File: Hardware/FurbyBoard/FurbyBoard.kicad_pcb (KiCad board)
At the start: 4 copper layers, 68.8 x 74.6 mm, 154 parts, among them J1 USB-C 16P, J11 J_EXP: header de expansión 2 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, J2 BAT+, J3 BAT-, J5 Micro I2S (SD, GND, SCK, WS, 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, J6 FPC 24P 0.5, J7 Frente: IR (emisor ×2, recept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, J8 Inclinación ×3, lengua ×2, al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, J9 Encoder ×3, leva ×2, barriga 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, Q1 SI7615ADN, Q3 AO3400A, SW1 RESET, SW2 BOOT, U1 USBLC6-2SC6, U10 TCA9535PWR, U11 SN74LVC1G17DBVR, U2 BQ24073RGTR, U3 TPS63802DLAR, U4 ESP32-S3-WROOM-1-N16R8, U5 TPS61089RNRR, U6 DRV8231ADSGR, U7 MAX98357AETE+T, U8 ME6211C28M5G-N, U9 ME6211C12M5G-N

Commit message: Feature: rutado de los sensores de J8 (TILT_A, TILT_B, TONGUE, sus series y el 3V3 de sus pull-ups)
- Bloque RC junto a U10: columna izquierda 0,3 mm al oeste para que quepa una columna de vías
  de 0,6 entre columnas (x -97,15); filas reordenadas (TILT_A, TILT_B, TONGUE) y cinco piezas a 180°.
- TILT_A por el hueco de filas y -78,25 y el pasillo junto a U10 a U10.4; TILT_B recto por y -80,015
  a U10.5; TONGUE por y -81,65 a U10.6. Series TILT_A_PAD, TILT_B_PAD y TONGUE_PAD por vías a B.Cu
  con carriles anidados hasta J8.1, J8.2 y J8.4.
- 3V3 de R45 a R38.2 (0,4 mm por el hueco de 0,75: dos avisos de 0,175 aceptados); R47 y R43 por
  vías a In2 hasta el tronco de 3V3 de B.Cu. TP14 (GND) a (-98,3; -86,4) para liberar B.Cu.

Puerta D: revisar-rutado 0 errores (86 avisos: cuellos, entradas asimétricas y rodeos heredados,
más 3 roces de 0,175-0,2 del 3V3 de R45), DRC paridad 0 y solo las 5 vías colgantes de redes
pendientes (CAM_EN, CAM_PWDN, I2C a J6); 68 sin unir. PNG revisado: zona U10/J8 (mapa con rejilla).

Co-Authored-By: Claude Opus 5.5 (1M context) <noreply@anthropic.com>
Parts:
- moved TP14 7.42 mm to (121.7, 46.4)
- moved C35 4.67 mm to (124.6, 40.8), turned to 180 degrees
- moved C36 3.89 mm to (121.1, 39.1), turned to 180 degrees
- moved R46 3.89 mm to (121.1, 37.4)
- moved R43 3.62 mm to (124.6, 42.5), turned to 180 degrees
- moved R44 3.62 mm to (124.6, 44.2), turned to 180 degrees
- moved C37 3.41 mm to (121.1, 42.5)
- moved R48 3.41 mm to (121.1, 40.8)
- moved R47 3.40 mm to (124.6, 39.1), turned to 180 degrees
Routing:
- net 3V3: track 210.8 -> 237.0 mm, vias 15 -> 18
- net TILT_B_PAD: track 0.00 -> 13.1 mm, vias 0 -> 1
- net TILT_A_PAD: track 0.00 -> 12.3 mm, vias 0 -> 1
- net TONGUE_PAD: track 0.00 -> 11.5 mm, vias 0 -> 1
- net TILT_A: track 0.00 -> 10.6 mm
- net TILT_B: track 0.00 -> 10.5 mm
- net TONGUE: track 0.00 -> 6.31 mm
- net GND: track 86.1 -> 85.2 mm, vias 102 -> 101
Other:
- board text removed: "SD"
- board text removed: "WS"

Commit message: Feature: rutado de los LED del frente, ENC_LED_A, BAT_G y 3V3 locales (R57/R58/R19, R17, TP6)
- LED PWR/RUN/PROG: ánodos rectos a su resistencia; LED_PWR_K por el norte de los LED (y -61,7,
  fuera del área de la antena) y x -52,9 hasta JP5.1.
- 3V3 de R57/R58/R19 por una fila de 0,4 (y -66,0) con vía a In2 (x -55,0) hasta la fila de 3V3
  de In2; la vía de GND de SW2.2 pasa al este (1,5 mm) para dejar sitio. R17.2 al 3V3 de C9/U4.2;
  TP6 unido al tronco de B.Cu (que acababa en y -107,3).
- ENC_LED_A entre las columnas de J9 hasta J9.3. BAT_G de la puerta de Q1 a R12 (0,5 mm dentro
  del patio de Q1 por la regla «cuello Q1»).

Puerta D: revisar-rutado 0 errores (102 avisos; nuevos: 2 roces de 0,15 de LED_PWR_K con D3.1
y JP5.2), DRC paridad 0 y 0 infracciones salvo las 5 vías colgantes de redes pendientes;
57 sin unir. PNG revisados: zona LED/JP5 y zona Q1/R12.

Co-Authored-By: Claude Opus 5.5 (1M context) <noreply@anthropic.com>
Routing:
- net 3V3: track 237.0 -> 269.5 mm, vias 18 -> 19
- net LED_PWR_K: track 0.00 -> 18.4 mm
- net ENC_LED_A: track 0.00 -> 8.81 mm
- net BAT_G: track 0.00 -> 2.80 mm
- net LED_RUN_A: track 0.00 -> 1.95 mm
- net LED_PWR_A: track 0.00 -> 1.95 mm
- net LED_PROG_A: track 0.00 -> 1.92 mm

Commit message: Feature: FurbyBoard a 6 capas (JLC06161H-7628) conservando el rutado: In3 señal, In4 GND, apilado en el PCB y en NOTAS
Decisión de Guillermo (2026-10-24 23:25) tras el diagnóstico del rutado en 4 capas. Mismo prepreg
exterior 7628 (0,2104 mm), así el par USB conserva sus ≈ 87 Ω sin tocar pistas. Keepout de la antena
en las 6 capas, plano de GND en In4, tipos de capa desde params.LAYER_TYPES, bloque (stackup) escrito
por gen_pcb.py, Gerber con In3/In4 en make_fab.sh. DRC: 0 infracciones salvo las 5 vías colgantes de
redes pendientes, paridad 0, 57 sin unir (igual que antes); revisar-rutado PASS (0 errores, 102 avisos).

Co-Authored-By: Claude Opus 5.5 (1M context) <noreply@anthropic.com>
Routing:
- added copper zone on In4.Cu, net GND
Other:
- copper layers 4 -> 6

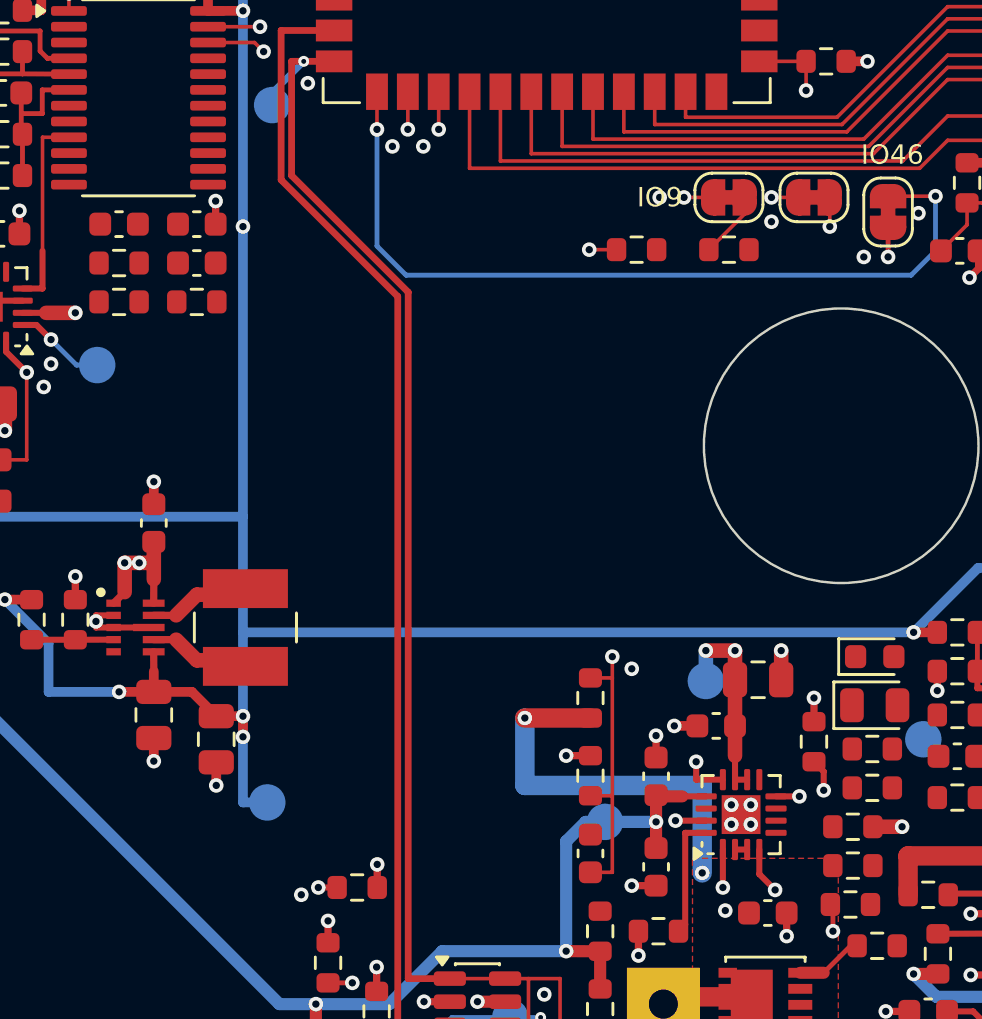
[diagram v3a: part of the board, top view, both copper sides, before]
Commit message: Feature: rutado de EN_6V, BQ_EN1 y BQ_EN2 desde U10 por In3
Vías bajo el cuerpo de U10 y pasillo NE en In3: bajada a más de 1 mm de las
columnas del I2S, cruce a 90° de VBAT_SNS y diagonal paralela a 1,2 mm por su
lado NE, al sur del agujero del mecanismo y bajada entre la vía de BQ_ILIM y
los LED del cargador. Llegada a U2 por vías en el eje de R6.1 y R7.1 (0,25 mm
dentro del patio de U2, regla «cuello U2»).

Puerta: revisar-rutado PASS (0 errores, 103 avisos; nuevo solo
entrada-asimetrica de R6 por el lado de VSYS). DRC con paridad 0 y sin
violaciones nuevas; BQ_EN1, BQ_EN2 y EN_6V sin conexiones pendientes.
PNG revisados: In3 del pasillo NE, F.Cu bajo U10 y F.Cu de U2.

Co-Authored-By: Claude Opus 5.5 (1M context) <noreply@anthropic.com>
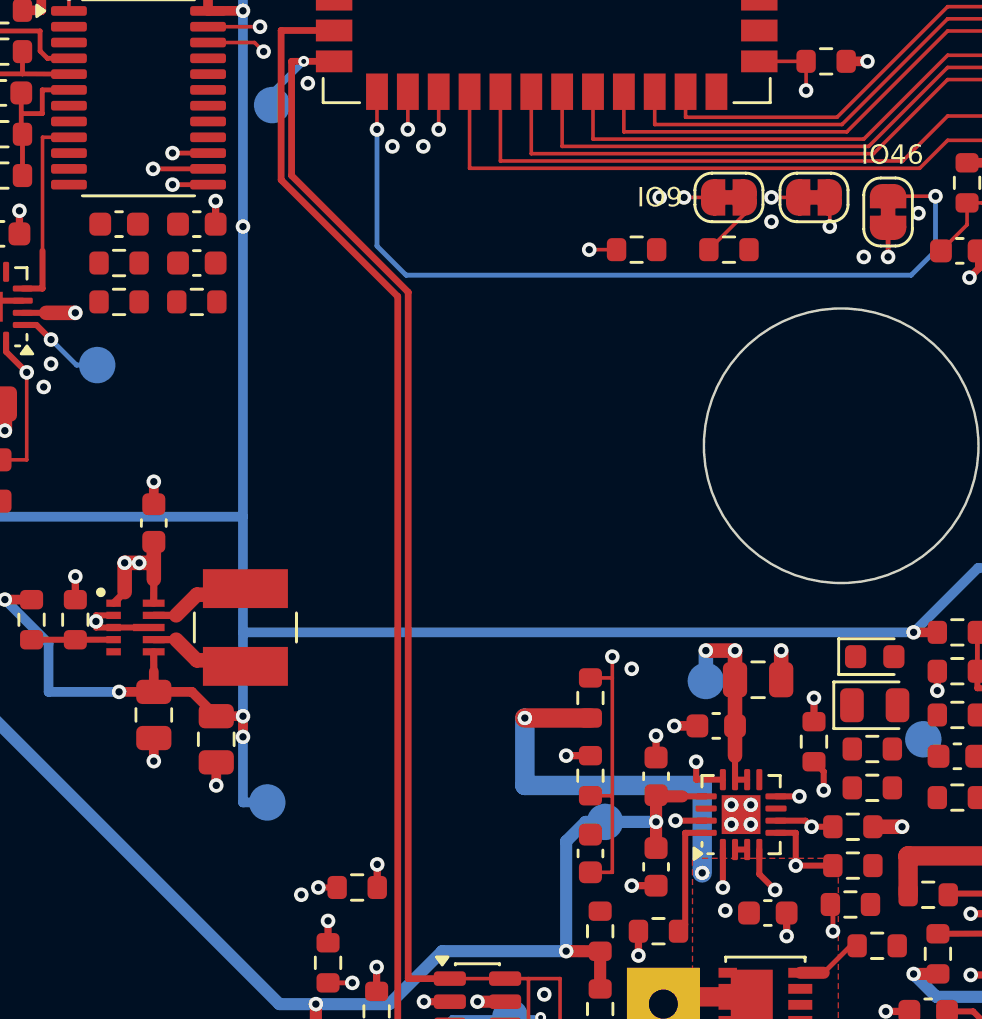
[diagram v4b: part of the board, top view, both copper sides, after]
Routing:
- net BQ_EN2: track 0.00 -> 59.3 mm, vias 0 -> 2
- net EN_6V: track 19.5 -> 76.2 mm, vias 2 -> 3
- net BQ_EN1: track 0.00 -> 52.7 mm, vias 0 -> 2

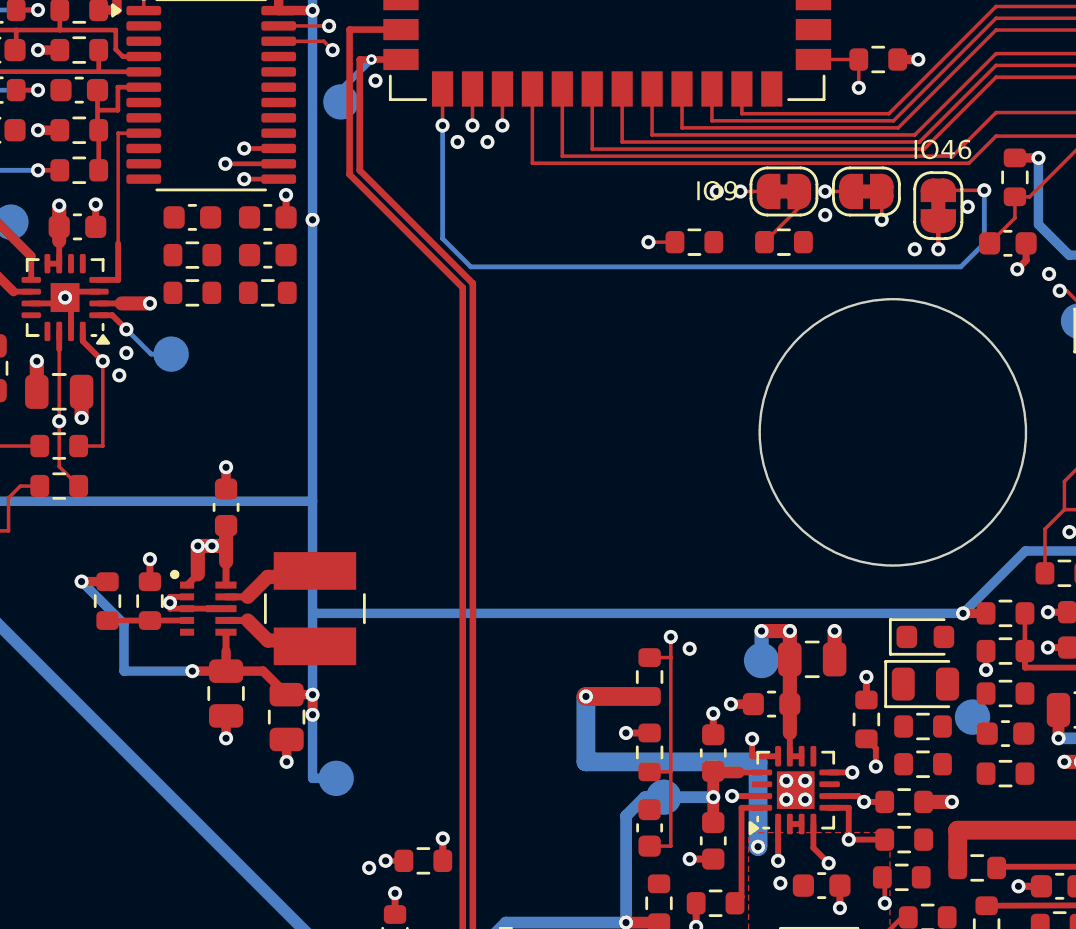
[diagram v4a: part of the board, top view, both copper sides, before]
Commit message: Feature: rutado de CHG y PGOOD desde U10 por In3 hasta el cargador
Vías bajo U10 y pasillo SO de In3 (bajada bajo U10, x -87,0/-86,55 y este en
y -105,6/-105,15, al sur de la vía de VBAT_SNS). C17 cierra el norte de U2.9:
CHG llega a su vía y un tramo corto de B.Cu la une a otra vía al oeste de D1.1,
de la que salen D1.1 y el carril x -61,225 hasta R9.1. PGOOD: U2.7 a R8.1 por
debajo con vía al norte del tramo; D2.1 cuelga de una vía entre los pads de
D1/D2 unida por B.Cu (en In3 cruzaría las bajadas de BQ_EN1/BQ_EN2/EN_6V). La
vía de GND de U2.8 sube en diagonal a (-63,2, -108,95) para dejar sitio.

Puerta: revisar-rutado PASS (0 errores, 104 avisos; nuevos: PGOOD a 0,175 de
R6.1 y la entrada asimétrica de R6). DRC con paridad 0, sin violaciones
nuevas; las cinco redes del bloque sin conexiones pendientes (46 en la placa).
PNG revisados: In3 de los pasillos SO y NE, F.Cu y B.Cu de U2, F.Cu bajo U10.

Co-Authored-By: Claude Opus 5.5 (1M context) <noreply@anthropic.com>
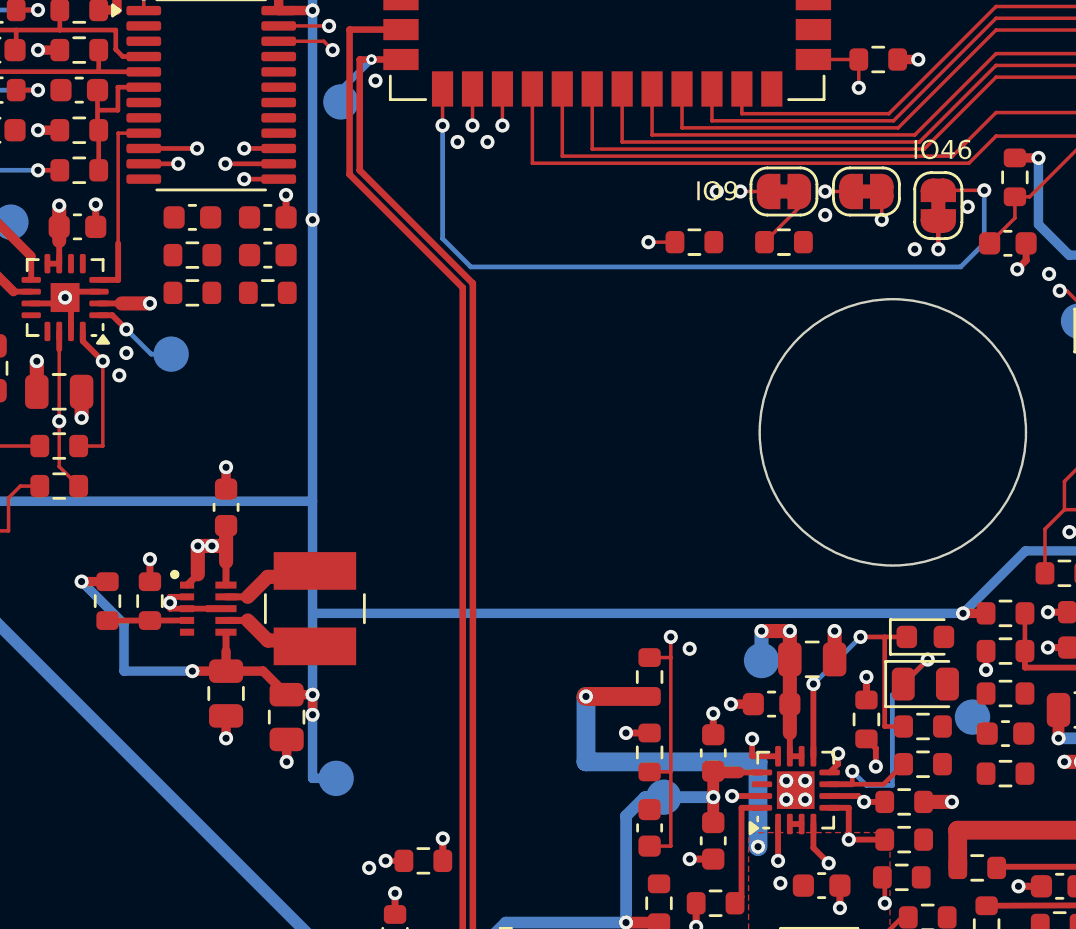
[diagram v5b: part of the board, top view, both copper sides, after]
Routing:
- net PGOOD: track 0.00 -> 69.9 mm, vias 0 -> 3
- net CHG: track 0.00 -> 62.9 mm, vias 0 -> 3
